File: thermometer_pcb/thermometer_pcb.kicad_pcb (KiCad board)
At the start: 2 copper layers, 76.9 x 49 mm, 23 parts, among them J1 POWER_IN, J2 TC_IN, J3 EXT_DS1, J4 EXT_DS2, J5 DISP, J6 Conn_01x02, J7 SPI, J8 I2C, J9 ENC, Q1 PN2222A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

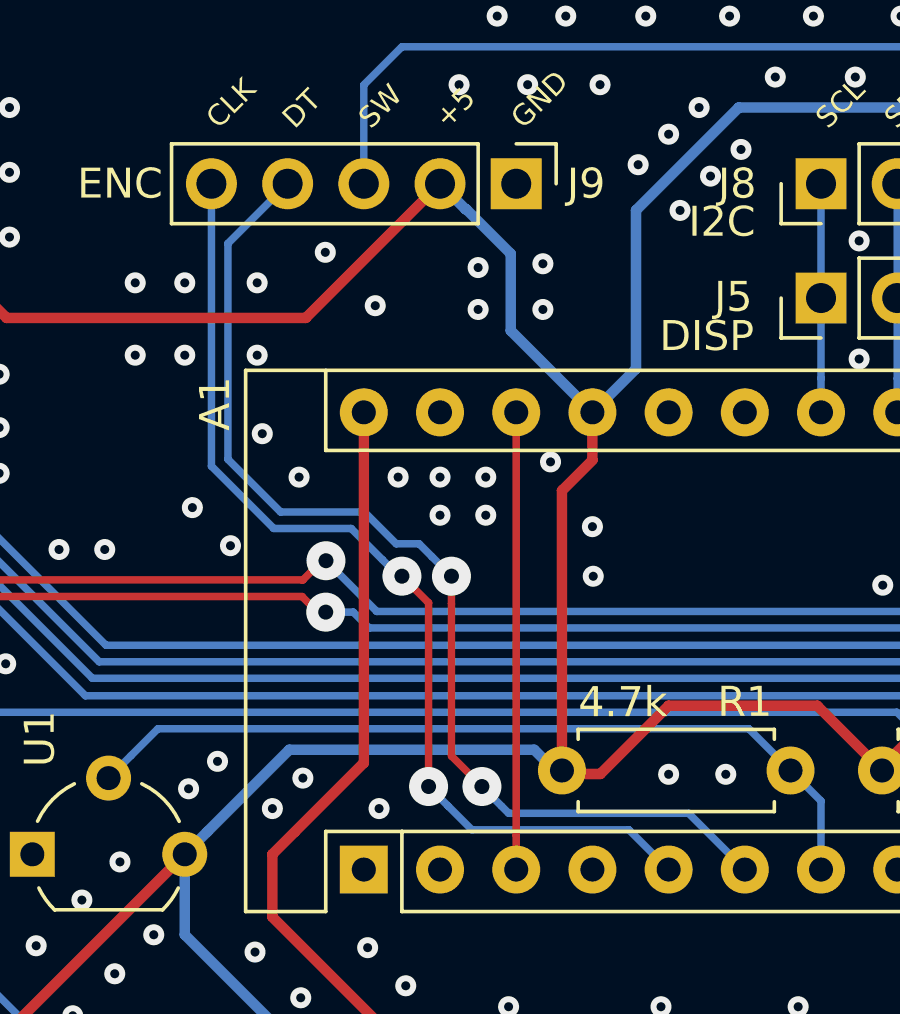
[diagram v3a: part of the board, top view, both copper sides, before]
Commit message: pcb: use nicro-via for CLK and DT encoder lines
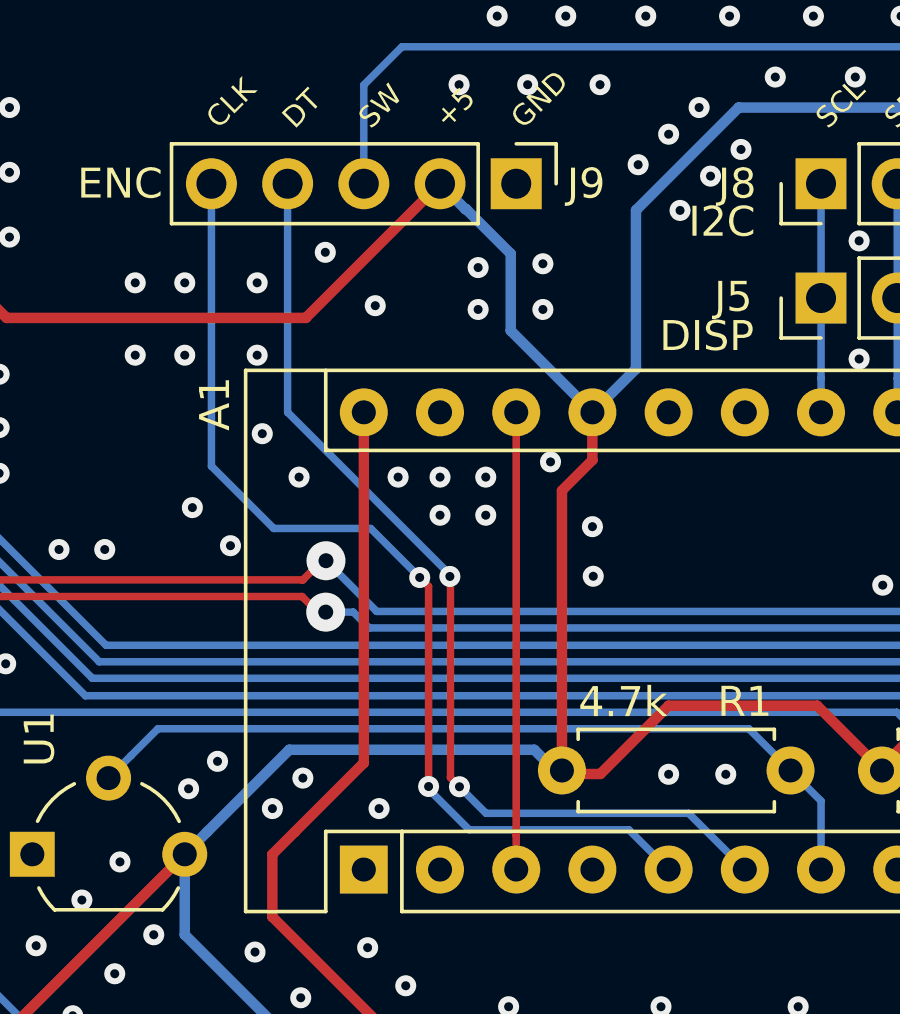
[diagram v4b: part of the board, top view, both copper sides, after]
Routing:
- net /3(**): track 36.4 -> 33.1 mm
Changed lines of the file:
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@@
     (thickness 1.6)
     (drawings 76)
-    (tracks 424)
+    (tracks 416)
     (modules 23)
     (nets 26)
@@
   (gr_line (start 216.416676 89.748604) (end 216.415641 84.398259) (layer "Edge.Cuts") (width 0.1))
   (gr_line (start 222.396676 75.698604) (end 222.396676 47.298604) (layer "Edge.Cuts") (width 0.1))
+  (segment (start 191.543676 72.933603) (end 186.221675 72.933603) (width 0.25) (layer "B.Cu") (net 13))
+  (segment (start 192.868677 74.258604) (end 191.543676 72.933603) (width 0.25) (layer "B.Cu") (net 13))
+  (segment (start 186.221675 72.933603) (end 184.867671 71.579599) (width 0.25) (layer "B.Cu") (net 13))
+  (segment (start 184.867671 71.579599) (end 184.867671 71.490732) (width 0.25) (layer "B.Cu") (net 13))
+  (segment (start 185.576676 64.488604) (end 185.596676 64.508604) (width 0.25) (layer "F.Cu") (net 21))
+  (via micro (at 185.576676 64.488604) (size 0.7) (drill 0.3) (layers "F.Cu" "B.Cu") (net 21))
+  (segment (start 180.168677 59.01856) (end 180.168677 51.398604) (width 0.25) (layer "B.Cu") (net 21))
+  (segment (start 185.576676 64.488604) (end 185.576676 64.426559) (width 0.25) (layer "B.Cu") (net 21))
+  (segment (start 185.576676 64.426559) (end 180.168677 59.01856) (width 0.25) (layer "B.Cu") (net 21))
+  (segment (start 185.596676 64.508604) (end 185.596676 71.198604) (width 0.25) (layer "F.Cu") (net 21))
+  (segment (start 185.596676 71.198604) (end 185.896676 71.498604) (width 0.25) (layer "F.Cu") (net 21))
+  (segment (start 177.628677 60.812437) (end 177.628677 51.398604) (width 0.25) (layer "B.Cu") (net 13))
+  (segment (start 184.571676 64.523604) (end 182.937717 62.889645) (width 0.25) (layer "B.Cu") (net 13))
+  (segment (start 179.705885 62.889645) (end 177.628677 60.812437) (width 0.25) (layer "B.Cu") (net 13))
+  (segment (start 182.937717 62.889645) (end 179.705885 62.889645) (width 0.25) (layer "B.Cu") (net 13))
+  (segment (start 184.571676 64.523604) (end 184.867671 64.819599) (width 0.25) (layer "F.Cu") (net 13))
+  (segment (start 184.867671 64.819599) (end 184.867671 71.490732) (width 0.25) (layer "F.Cu") (net 13))
+  (via micro (at 184.571676 64.523604) (size 0.7) (drill 0.3) (layers "F.Cu" "B.Cu") (net 13))
+  (segment (start 195.408677 74.258604) (end 193.533665 72.383592) (width 0.25) (layer "B.Cu") (net 21))
+  (segment (start 186.781664 72.383592) (end 185.896676 71.498604) (width 0.25) (layer "B.Cu") (net 21))
+  (segment (start 193.533665 72.383592) (end 186.781664 72.383592) (width 0.25) (layer "B.Cu") (net 21))
+  (via micro (at 185.896676 71.498604) (size 0.7) (drill 0.3) (layers "F.Cu" "B.Cu") (net 21))
   (via micro (at 155.896676 47.598604) (size 0.7) (drill 0.3) (layers "F.Cu" "B.Cu") (net 1))
   (segment (start 149.611177 57.395104) (end 151.200176 57.395104) (width 0.25) (layer "B.Cu") (net 3))
@@
   (via micro (at 161.499677 53.938604) (size 0.7) (drill 0.3) (layers "F.Cu" "B.Cu") (net 1))
   (via micro (at 161.753677 55.829614) (size 0.7) (drill 0.3) (layers "F.Cu" "B.Cu") (net 1))
-  (via (at 183.978677 64.479604) (size 1.3) (drill 0.5) (layers "F.Cu" "B.Cu") (net 13) (status 40000))
-  (segment (start 177.628677 60.812437) (end 179.705885 62.889645) (width 0.25) (layer "B.Cu") (net 13) (status 40000))
-  (segment (start 177.628677 51.398604) (end 177.628677 60.812437) (width 0.25) (layer "B.Cu") (net 13) (status 40000))
-  (segment (start 179.705885 62.889645) (end 182.288375 62.889645) (width 0.25) (layer "B.Cu") (net 13) (status 40000))
-  (segment (start 182.288375 62.889645) (end 183.328678 63.929947) (width 0.25) (layer "B.Cu") (net 13))
-  (segment (start 183.328678 63.929947) (end 183.978677 64.579946) (width 0.25) (layer "B.Cu") (net 13) (status 40000))
-  (via (at 186.645677 71.490644) (size 1.3) (drill 0.5) (layers "F.Cu" "B.Cu") (net 21))
-  (segment (start 195.408677 74.258604) (end 193.533665 72.383592) (width 0.25) (layer "B.Cu") (net 21))
-  (segment (start 193.533665 72.383592) (end 187.538625 72.383592) (width 0.25) (layer "B.Cu") (net 21))
-  (segment (start 187.538625 72.383592) (end 187.295676 72.140643) (width 0.25) (layer "B.Cu") (net 21))
-  (segment (start 187.295676 72.140643) (end 186.645677 71.490644) (width 0.25) (layer "B.Cu") (net 21))
   (via micro (at 179.152677 57.113604) (size 0.7) (drill 0.3) (layers "F.Cu" "B.Cu") (net 1))
   (via micro (at 179.152677 54.700604) (size 0.7) (drill 0.3) (layers "F.Cu" "B.Cu") (net 1))
@@
   (segment (start 189.196277 71.073004) (end 188.388899 70.265626) (width 0.35) (layer "B.Cu") (net 2))
   (segment (start 203.028677 71.565804) (end 203.028677 73.127234) (width 0.25) (layer "B.Cu") (net 18))
-  (via (at 184.867671 71.490732) (size 1.3) (drill 0.5) (layers "F.Cu" "B.Cu") (net 13))
+  (via micro (at 184.867671 71.490732) (size 0.7) (drill 0.3) (layers "F.Cu" "B.Cu") (net 13))
   (segment (start 159.350797 69.015604) (end 200.478477 69.015604) (width 0.25) (layer "B.Cu") (net 18))
   (segment (start 180.224655 70.265626) (end 177.489676 73.000605) (width 0.35) (layer "B.Cu") (net 2))
   (segment (start 200.478477 69.015604) (end 203.028677 71.565804) (width 0.25) (layer "B.Cu") (net 18))
   (segment (start 177.489676 73.000605) (end 176.739677 73.750604) (width 0.35) (layer "B.Cu") (net 2))
-  (segment (start 192.868677 74.258604) (end 191.543676 72.933603) (width 0.25) (layer "B.Cu") (net 13))
-  (segment (start 191.543676 72.933603) (end 186.310542 72.933603) (width 0.25) (layer "B.Cu") (net 13))
-  (segment (start 185.51767 72.140731) (end 184.867671 71.490732) (width 0.25) (layer "B.Cu") (net 13))
   (segment (start 175.844666 69.565615) (end 174.949676 70.460605) (width 0.25) (layer "B.Cu") (net 12))
-  (segment (start 186.310542 72.933603) (end 185.51767 72.140731) (width 0.25) (layer "B.Cu") (net 13))
   (segment (start 195.541688 69.565615) (end 175.844666 69.565615) (width 0.25) (layer "B.Cu") (net 12))
   (segment (start 174.949676 70.460605) (end 174.199677 71.210604) (width 0.25) (layer "B.Cu") (net 12))
@@
   (via micro (at 167.849677 47.080604) (size 0.7) (drill 0.3) (layers "F.Cu" "B.Cu") (net 1))
   (via micro (at 170.552187 61.050604) (size 0.7) (drill 0.3) (layers "F.Cu" "B.Cu") (net 1))
-  (via (at 185.629677 64.479604) (size 1.3) (drill 0.5) (layers "F.Cu" "B.Cu") (net 21))
-  (segment (start 185.629721 65.398842) (end 185.629721 64.479604) (width 0.25) (layer "F.Cu") (net 21))
-  (segment (start 185.629721 70.474688) (end 185.629721 65.398842) (width 0.25) (layer "F.Cu") (net 21))
-  (segment (start 186.645677 71.490644) (end 185.629721 70.474688) (width 0.25) (layer "F.Cu") (net 21))
   (via micro (at 181.424687 53.684604) (size 0.7) (drill 0.3) (layers "F.Cu" "B.Cu") (net 1))
   (via micro (at 179.323493 59.729968) (size 0.7) (drill 0.3) (layers "F.Cu" "B.Cu") (net 1))
@@
   (via micro (at 206.965677 76.671604) (size 0.7) (drill 0.3) (layers "F.Cu" "B.Cu") (net 1))
   (via micro (at 209.632677 76.798604) (size 0.7) (drill 0.3) (layers "F.Cu" "B.Cu") (net 1))
-  (segment (start 184.867671 65.368598) (end 184.867671 71.490732) (width 0.25) (layer "F.Cu") (net 13))
-  (segment (start 183.978677 64.579946) (end 184.079019 64.579946) (width 0.25) (layer "F.Cu") (net 13))
-  (segment (start 184.079019 64.579946) (end 184.867671 65.368598) (width 0.25) (layer "F.Cu") (net 13))
-  (segment (start 184.979722 63.829605) (end 185.629721 64.479604) (width 0.25) (layer "B.Cu") (net 21))
-  (segment (start 184.550199 63.400082) (end 184.979722 63.829605) (width 0.25) (layer "B.Cu") (net 21))
-  (segment (start 180.168677 51.398604) (end 178.178687 53.388594) (width 0.25) (layer "B.Cu") (net 21))
-  (segment (start 178.178687 60.584617) (end 179.933705 62.339635) (width 0.25) (layer "B.Cu") (net 21))
-  (segment (start 183.788155 63.400082) (end 184.550199 63.400082) (width 0.25) (layer "B.Cu") (net 21))
-  (segment (start 178.178687 53.388594) (end 178.178687 60.584617) (width 0.25) (layer "B.Cu") (net 21))
-  (segment (start 182.727708 62.339635) (end 183.788155 63.400082) (width 0.25) (layer "B.Cu") (net 21))
-  (segment (start 179.933705 62.339635) (end 182.727708 62.339635) (width 0.25) (layer "B.Cu") (net 21))
   (via micro (at 200.005677 64.779974) (size 0.7) (drill 0.3) (layers "F.Cu" "B.Cu") (net 1))
   (via micro (at 190.355677 64.482604) (size 0.7) (drill 0.3) (layers "F.Cu" "B.Cu") (net 1))

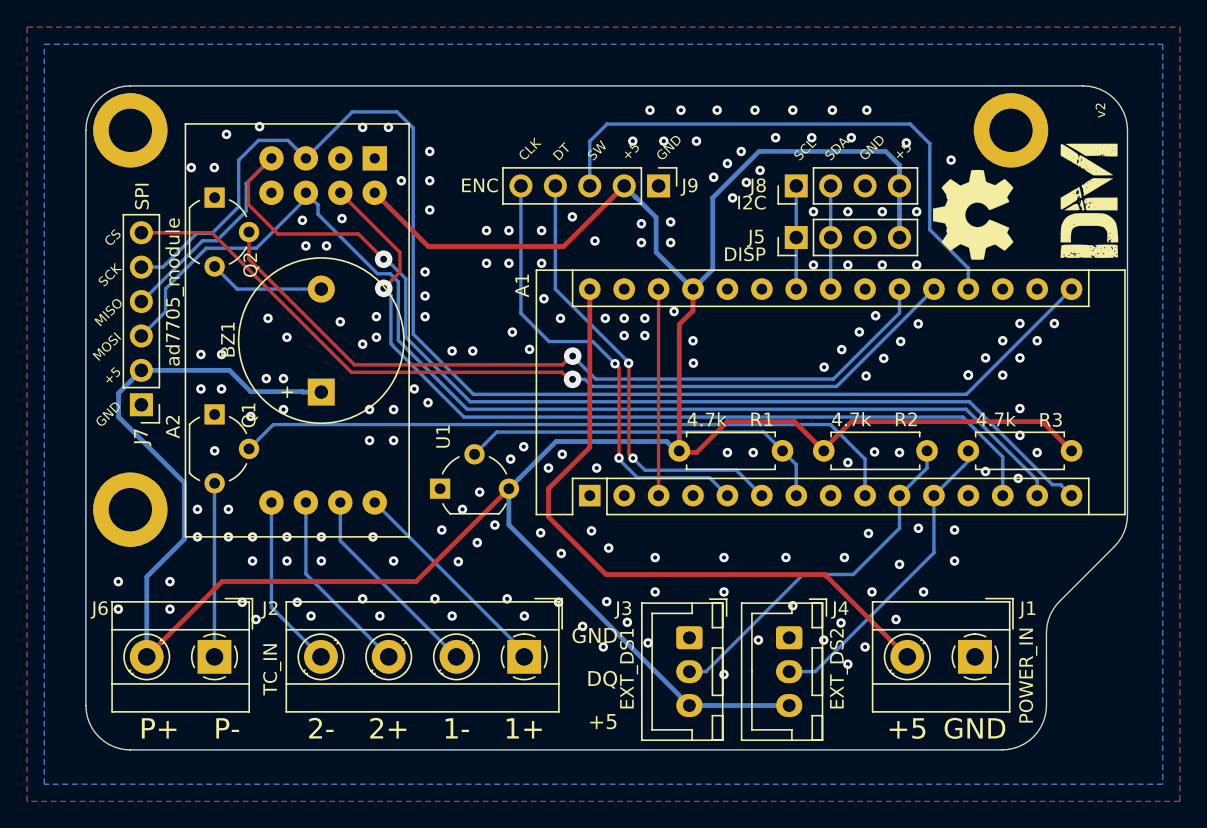
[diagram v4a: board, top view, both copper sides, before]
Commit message: pcb: use micro-via for SS, MISO, A1, A2 lines
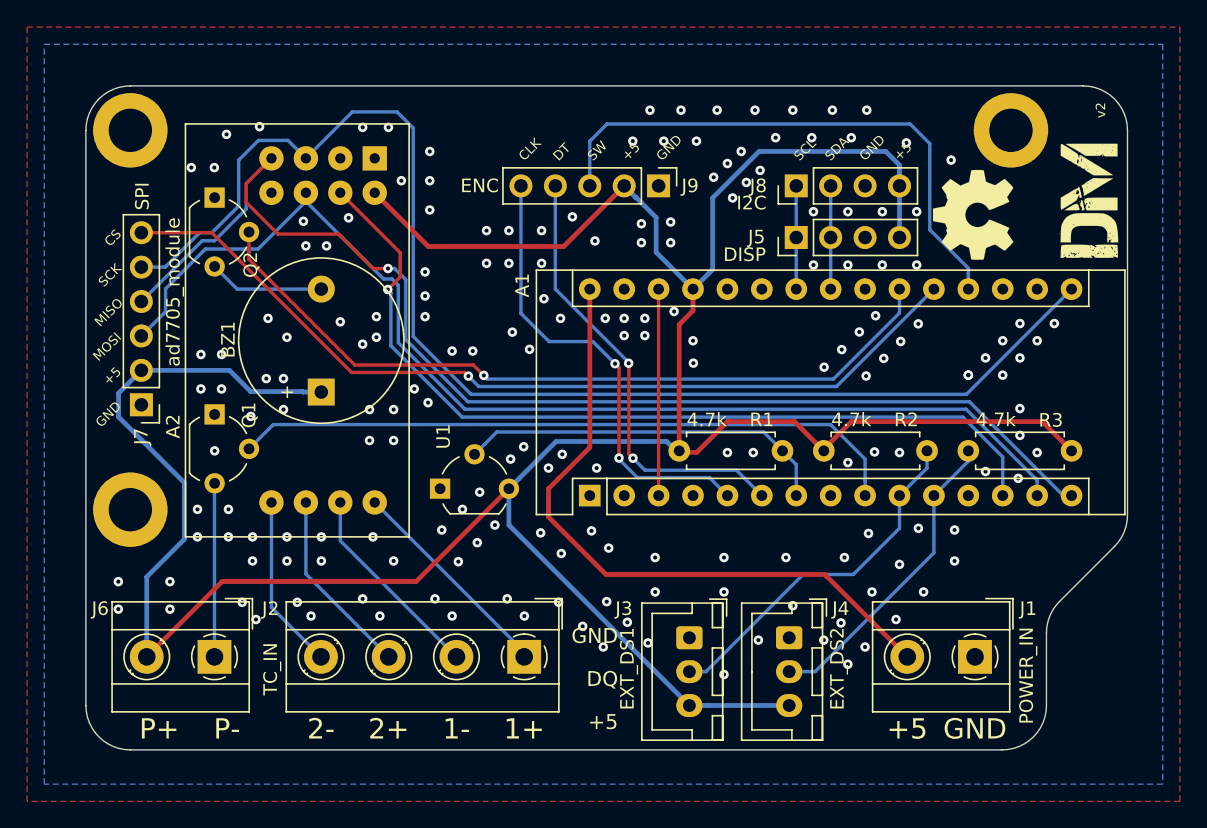
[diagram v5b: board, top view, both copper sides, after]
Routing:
- net /A2: track 58.0 -> 57.5 mm

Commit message: pcb: change dimensions
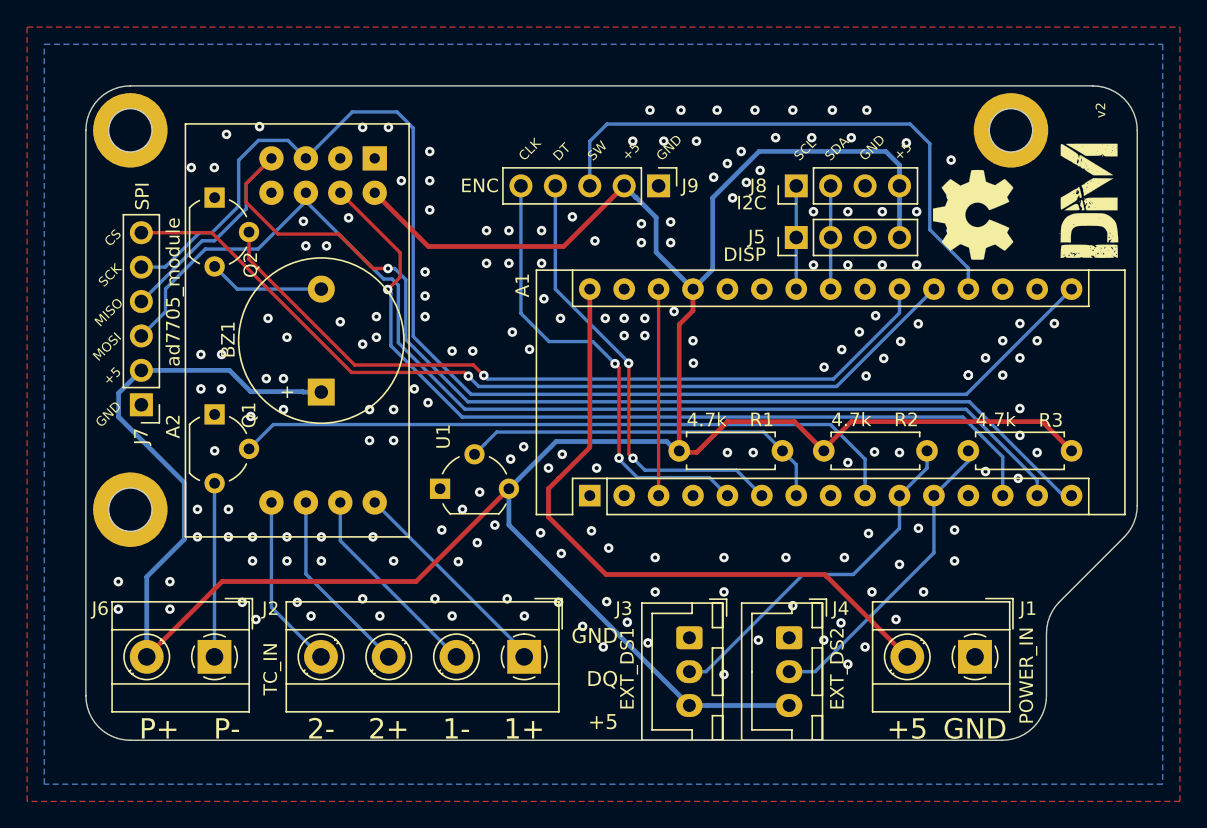
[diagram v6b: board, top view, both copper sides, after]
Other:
- board size 76.9 x 49 mm -> 77.6 x 48.3 mm
